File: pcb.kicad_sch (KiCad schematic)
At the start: 14 parts

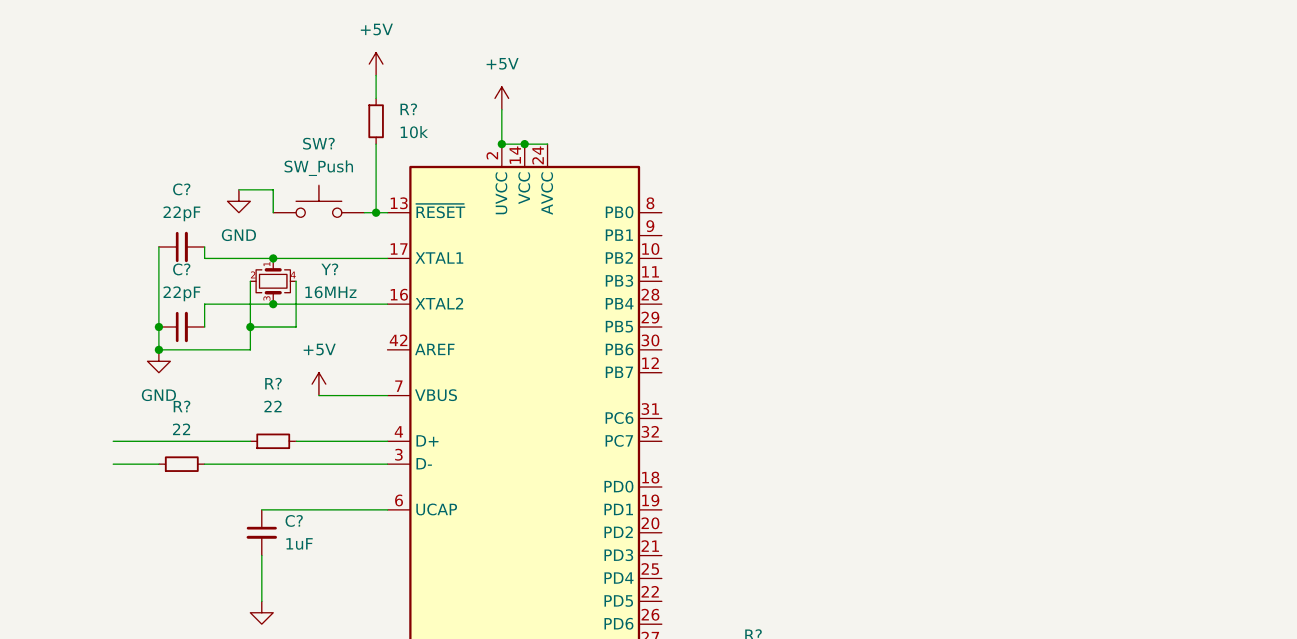
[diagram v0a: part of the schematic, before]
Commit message: start type c work
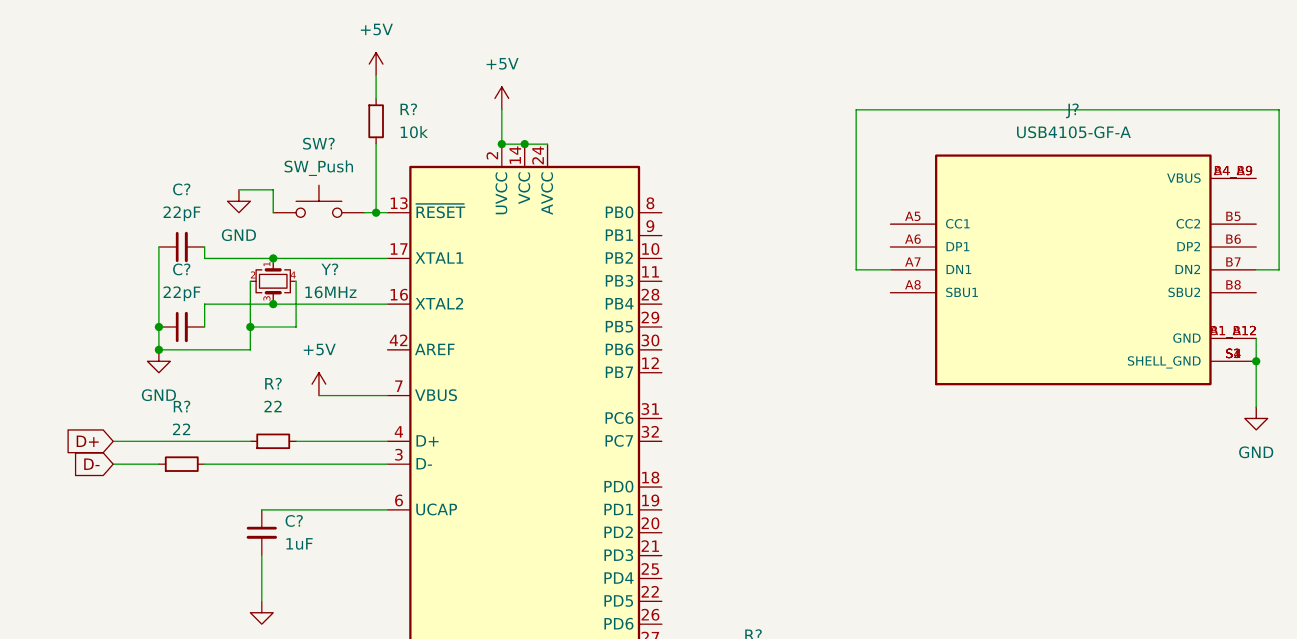
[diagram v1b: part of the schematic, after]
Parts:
- added J?: USB4105-GF-A, GCT_USB4105-GF-A, symbol USB4105-GF-A:USB4105-GF-A
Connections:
- net +5V: now also J?.A1_B12 (GND), J?.B1_A12 (GND), J?.S1 (SHELL_GND), J?.S2 (SHELL_GND), J?.S3 (SHELL_GND), J?.S4 (SHELL_GND)
- net D-: now reaches R?.1
- net D+: now reaches R?.1
- new net: J?.A4_B9 (VBUS), J?.B4_A9 (VBUS)
- new net: J?.A7 (DN1), J?.B7 (DN2)
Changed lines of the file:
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@@
   (junction (at 69.85 66.04) (diameter 0) (color 0 0 0 0)
   )
+  (junction (at 167.64 82.55) (diameter 0) (color 0 0 0 0)
+  )
   (junction (at 83.82 58.42) (diameter 0) (color 0 0 0 0)
   )
@@
     (stroke (width 0) (type default) (color 0 0 0 0))
   )
+  (wire (pts (xy 167.64 80.01) (xy 167.64 82.55))
+    (stroke (width 0) (type default) (color 0 0 0 0))
+  )
   (wire (pts (xy 74.93 149.86) (xy 83.82 149.86))
     (stroke (width 0) (type default) (color 0 0 0 0))
@@
     (stroke (width 0) (type default) (color 0 0 0 0))
   )
+  (wire (pts (xy 170.18 72.39) (xy 167.64 72.39))
+    (stroke (width 0) (type default) (color 0 0 0 0))
+  )
   (wire (pts (xy 58.42 71.12) (xy 50.8 71.12))
     (stroke (width 0) (type default) (color 0 0 0 0))
   )
+  (wire (pts (xy 167.64 82.55) (xy 167.64 87.63))
+    (stroke (width 0) (type default) (color 0 0 0 0))
+  )
   (wire (pts (xy 55.88 78.74) (xy 55.88 81.28))
     (stroke (width 0) (type default) (color 0 0 0 0))
   )
+  (wire (pts (xy 123.19 54.61) (xy 170.18 54.61))
+    (stroke (width 0) (type default) (color 0 0 0 0))
+  )
   (wire (pts (xy 50.8 93.98) (xy 71.12 93.98))
     (stroke (width 0) (type default) (color 0 0 0 0))
@@
     (stroke (width 0) (type default) (color 0 0 0 0))
   )
+  (wire (pts (xy 170.18 54.61) (xy 170.18 72.39))
+    (stroke (width 0) (type default) (color 0 0 0 0))
+  )
   (wire (pts (xy 60.96 73.66) (xy 60.96 78.74))
     (stroke (width 0) (type default) (color 0 0 0 0))
@@
     (stroke (width 0) (type default) (color 0 0 0 0))
   )
+  (wire (pts (xy 127 72.39) (xy 123.19 72.39))
+    (stroke (width 0) (type default) (color 0 0 0 0))
+  )
   (wire (pts (xy 83.82 58.42) (xy 83.82 54.61))
     (stroke (width 0) (type default) (color 0 0 0 0))
@@
     (stroke (width 0) (type default) (color 0 0 0 0))
   )
+  (wire (pts (xy 123.19 54.61) (xy 123.19 72.39))
+    (stroke (width 0) (type default) (color 0 0 0 0))
+  )
   (wire (pts (xy 52.07 121.92) (xy 62.23 121.92))
     (stroke (width 0) (type default) (color 0 0 0 0))
@@
   (wire (pts (xy 58.42 71.12) (xy 71.12 71.12))
     (stroke (width 0) (type default) (color 0 0 0 0))
+  )
+  (global_label "D+" (shape input) (at 40.64 91.44 180) (fields_autoplaced)
+    (effects (font (size 1.27 1.27)) (justify right))
+    (property "Intersheet References" "${INTERSHEET_REFS}" (id 0) (at 35.3845 91.3606 0)
+      (effects (font (size 1.27 1.27)) (justify right) hide)
+    )
+  )
+  (global_label "D-" (shape input) (at 40.64 93.98 180) (fields_autoplaced)
+    (effects (font (size 1.27 1.27)) (justify right))
+    (property "Intersheet References" "${INTERSHEET_REFS}" (id 0) (at 35.3845 93.9006 0)
+      (effects (font (size 1.27 1.27)) (justify right) hide)
+    )
   )
   (symbol (lib_id "power:GND") (at 45.72 81.28 0) (unit 1)
@@
     )
     (pin "1")
+  )
+  (symbol (lib_id "USB4105-GF-A:USB4105-GF-A") (at 147.32 72.39 0) (unit 1)
+    (in_bom yes) (on_board yes) (fields_autoplaced)
+    (property "Reference" "J?" (id 0) (at 147.32 54.61 0))
+    (property "Value" "USB4105-GF-A" (id 1) (at 147.32 57.15 0))
+    (property "Footprint" "GCT_USB4105-GF-A" (id 2) (at 147.32 72.39 0)
+      (effects (font (size 1.27 1.27)) (justify left bottom) hide)
+    )
+    (property "Datasheet" "" (id 3) (at 147.32 72.39 0)
+      (effects (font (size 1.27 1.27)) (justify left bottom) hide)
+    )
+    (property "STANDARD" "Manufacturer Recommendations" (id 4) (at 147.32 72.39 0)
+      (effects (font (size 1.27 1.27)) (justify left bottom) hide)
+    )
+    (property "PARTREV" "A3" (id 5) (at 147.32 72.39 0)
+      (effects (font (size 1.27 1.27)) (justify left bottom) hide)
+    )
+    (property "MAXIMUM_PACKAGE_HEIGHT" "3.31 mm" (id 6) (at 147.32 72.39 0)
+      (effects (font (size 1.27 1.27)) (justify left bottom) hide)
+    )
+    (property "MANUFACTURER" "GCT" (id 7) (at 147.32 72.39 0)
+      (effects (font (size 1.27 1.27)) (justify left bottom) hide)
+    )
+    (pin "A1_B12")
+    (pin "A4_B9")
+    (pin "A5")
+    (pin "A6")
+    (pin "A7")
+    (pin "A8")
+    (pin "B1_A12")
+    (pin "B4_A9")
+    (pin "B5")
+    (pin "B6")
+    (pin "B7")
+    (pin "B8")
+    (pin "S1")
+    (pin "S2")
+    (pin "S3")
+    (pin "S4")
   )
   (symbol (lib_id "power:GND") (at 57.15 109.22 0) (unit 1)
@@
     (pin "2")
   )
+  (symbol (lib_id "power:GND") (at 167.64 87.63 0) (unit 1)
+    (in_bom yes) (on_board yes) (fields_autoplaced)
+    (property "Reference" "#PWR?" (id 0) (at 167.64 93.98 0)
+      (effects (font (size 1.27 1.27)) hide)
+    )
+    (property "Value" "GND" (id 1) (at 167.64 92.71 0))
+    (property "Footprint" "" (id 2) (at 167.64 87.63 0)
+      (effects (font (size 1.27 1.27)) hide)
+    )
+    (property "Datasheet" "" (id 3) (at 167.64 87.63 0)
+      (effects (font (size 1.27 1.27)) hide)
+    )
+    (pin "1")
+  )
   (symbol (lib_id "power:GND") (at 45.72 127 0) (unit 1)
     (in_bom yes) (on_board yes) (fields_autoplaced)
@@
       (reference "#PWR?") (unit 1) (value "GND") (footprint "")
     )
+    (path "/7fe8d1fc-4b3b-4547-b06f-7ec679b6a185"
+      (reference "#PWR?") (unit 1) (value "GND") (footprint "")
+    )
     (path "/80f52858-35bb-45ed-b02a-80c187a25783"
       (reference "#PWR?") (unit 1) (value "GND") (footprint "")
@@
       (reference "C?") (unit 1) (value "0.1uF") (footprint "")
     )
+    (path "/07524104-0ccc-4f33-96e3-078d327a1b00"
+      (reference "J?") (unit 1) (value "USB4105-GF-A") (footprint "GCT_USB4105-GF-A")
+    )
     (path "/3c282268-338d-41b5-accc-b93c90294946"

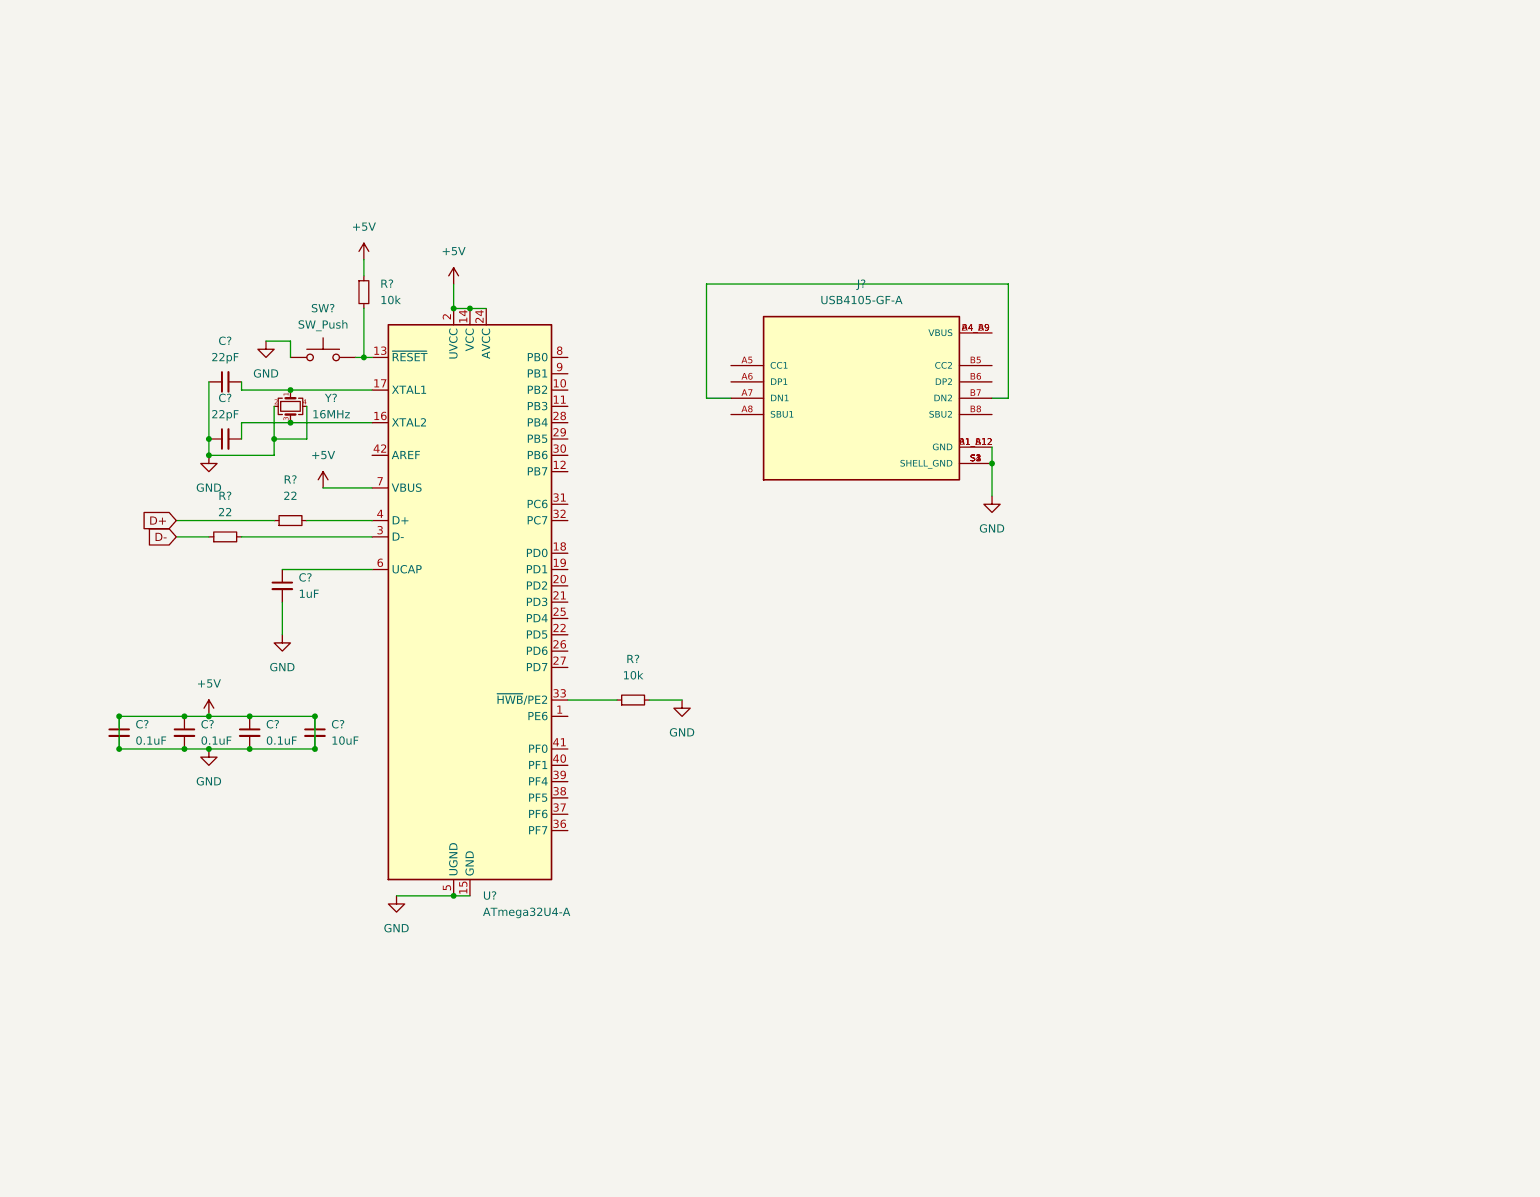
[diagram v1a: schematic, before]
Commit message: used mini-usb instead of usb-c because screw u ai03
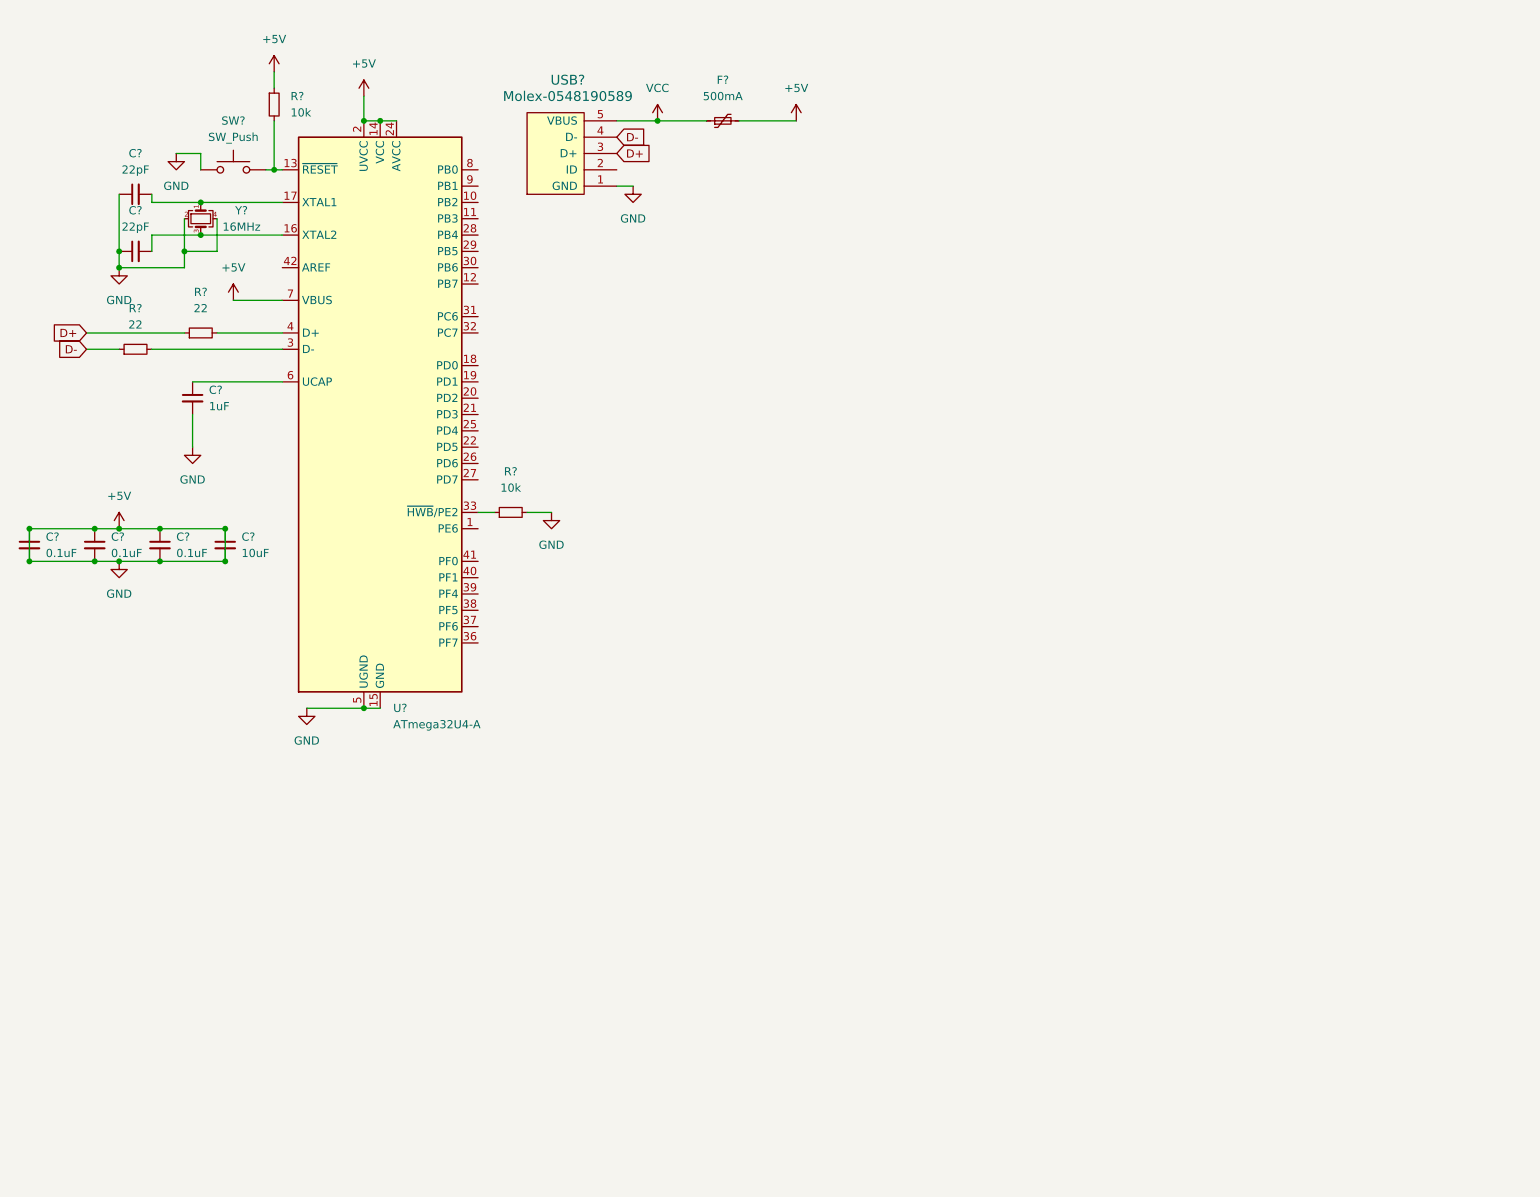
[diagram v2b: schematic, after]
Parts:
- removed J?: USB4105-GF-A, GCT_USB4105-GF-A, symbol USB4105-GF-A:USB4105-GF-A
- added F?: 500mA, symbol Device:Polyfuse_Small
- added USB?: Molex-0548190589, symbol random-keyboard-parts:Molex-0548190589
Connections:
- net +5V: now also F?.2, USB?.1 (GND)
- net D+: now also USB?.3 (D+)
- net D-: now also USB?.4 (D-)
- new net VCC: F?.1, USB?.5 (VBUS)
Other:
- moved on the sheet: C?, R?, SW?, U?, Y?

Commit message: started switch grid schematic
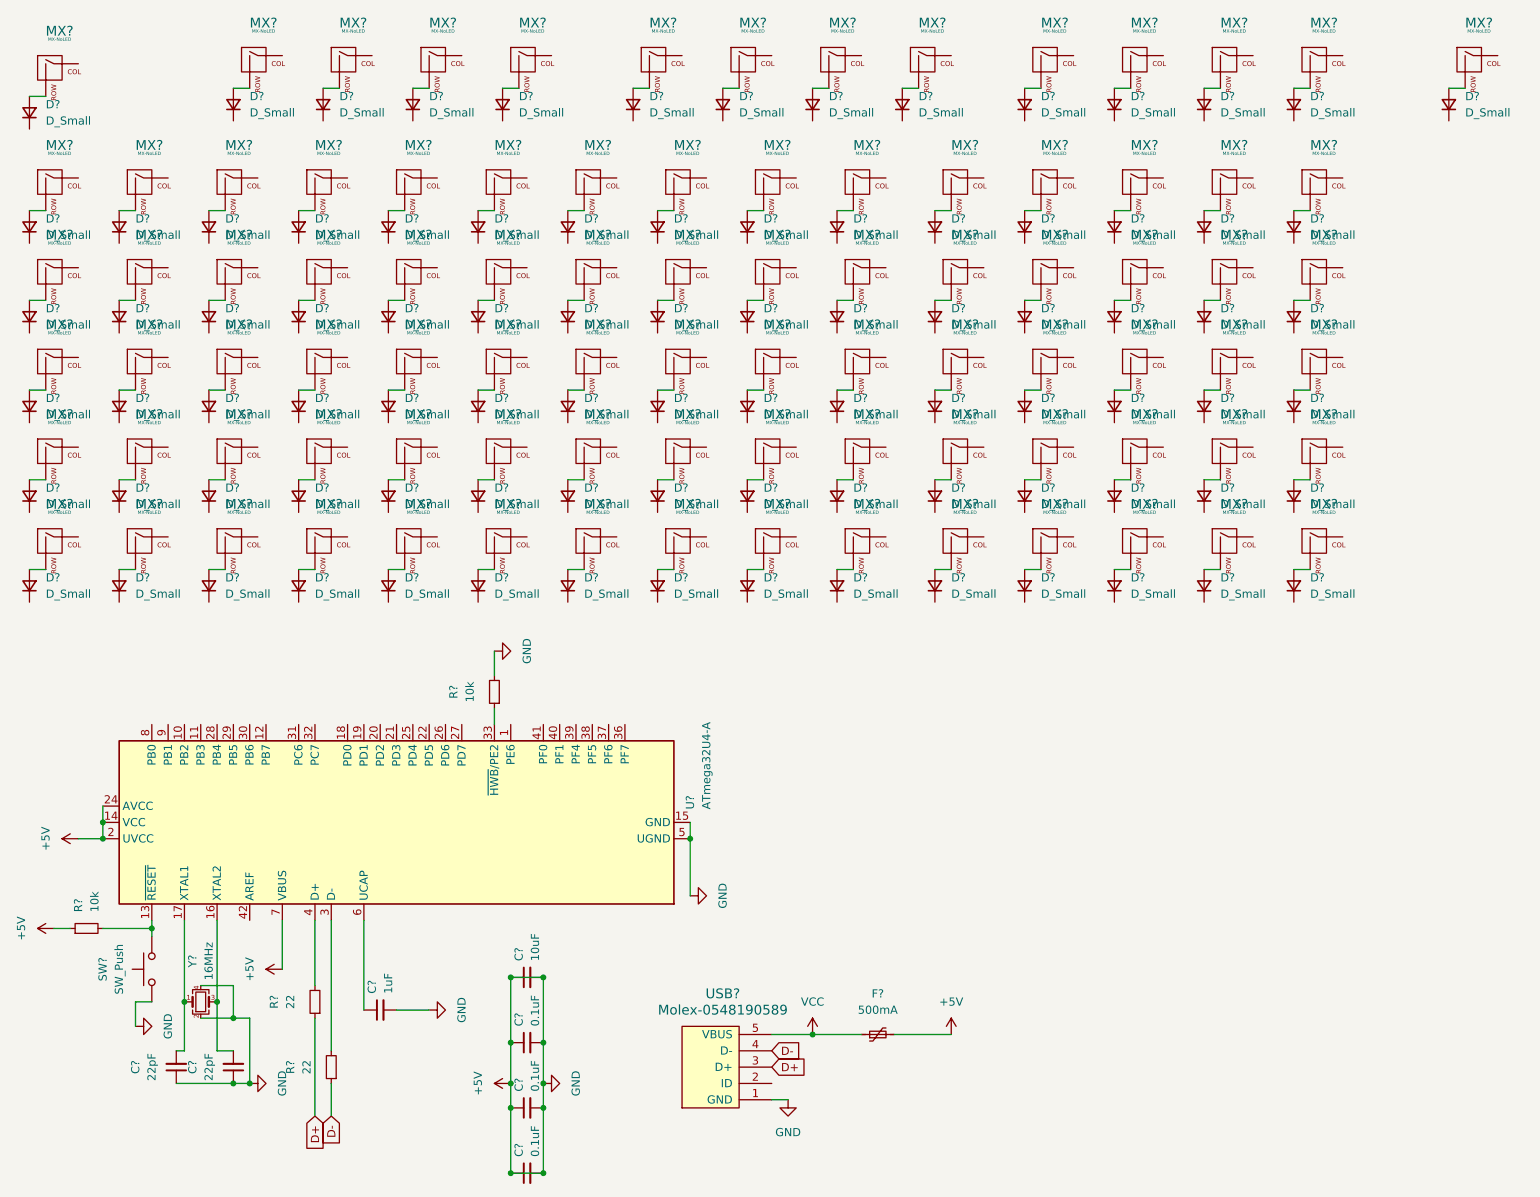
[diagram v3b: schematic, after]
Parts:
- added D? (x89): D_Small, symbol Device:D_Small
- added MX? (x89): MX-NoLED, symbol MX_Alps_Hybrid:MX-NoLED
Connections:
- new net: D?.2 (A), MX?.2 (ROW) (x89)
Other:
- moved on the sheet: C?, F?, R?, SW?, U?, USB?, Y?
